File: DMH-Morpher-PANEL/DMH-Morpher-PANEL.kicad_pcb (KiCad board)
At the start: 2 copper layers, 50 x 200 mm, 4 parts

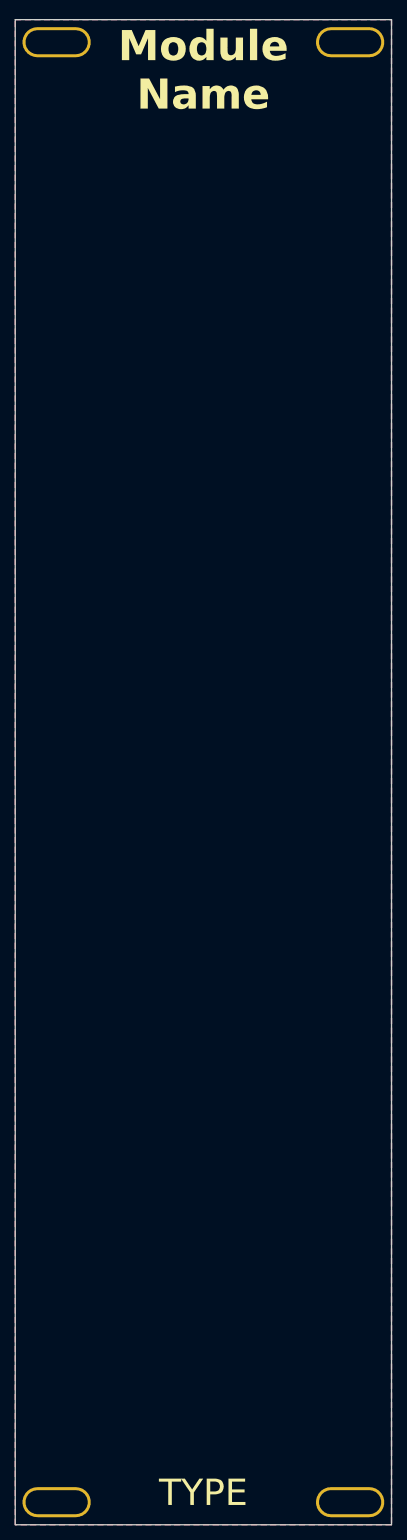
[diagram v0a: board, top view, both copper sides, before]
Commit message: Designed panel
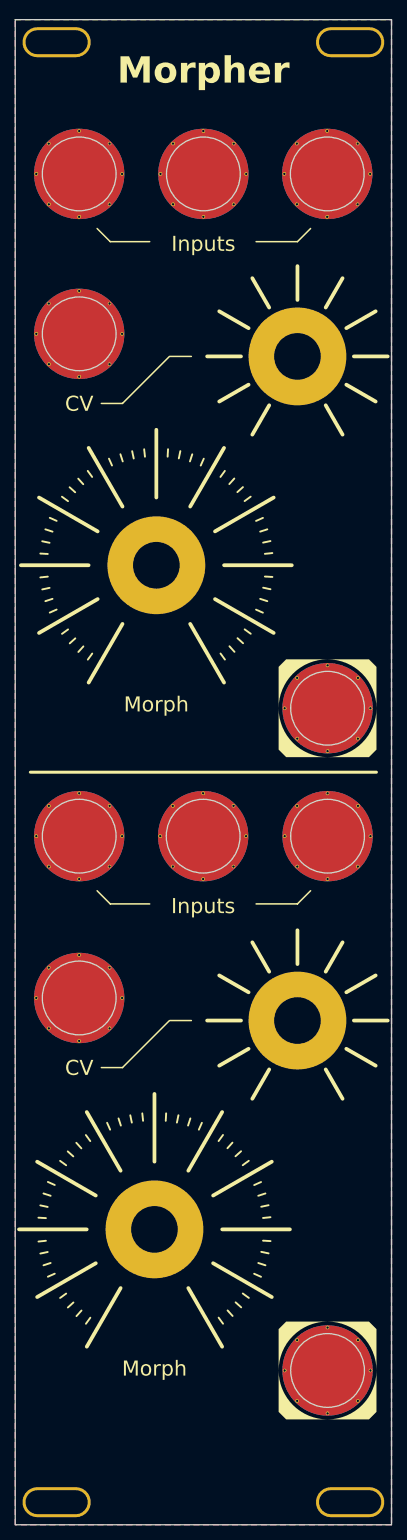
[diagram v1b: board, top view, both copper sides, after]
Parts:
- added H10: Morph, SynthStuff:Pot_Cutout_Medium_v2, F.Cu at (68.8, 102.5)
- added H11: CV A Amount, SynthStuff:Pot_Cutout_Tiny, F.Cu at (87.5, 74.8)
- added H12: In B1, SynthStuff:Jack_6.35mm_Cutout_v3, F.Cu at (58.5, 138.5)
- added H13: Out B, SynthStuff:Jack_6.35mm_Cutout_Output_v6, F.Cu at (91.5, 209.5)
- added H14: Morph, SynthStuff:Pot_Cutout_Medium_v2, F.Cu at (68.5, 190.8)
- added H15: Inputs, SynthStuff:Jack_6.35mm_Cutout_v3, F.Cu at (75.0, 138.5)
- added H16: CV B Amount, SynthStuff:Pot_Cutout_Tiny, F.Cu at (87.5, 163.0)
- added H17: In B3, SynthStuff:Jack_6.35mm_Cutout_v3, F.Cu at (91.5, 138.5)
- added H18: CV, SynthStuff:Jack_6.35mm_Cutout_v3, F.Cu at (58.5, 160.0)
- added H5: In A1, SynthStuff:Jack_6.35mm_Cutout_v3, F.Cu at (58.5, 50.5)
- added H6: Inputs, SynthStuff:Jack_6.35mm_Cutout_v3, F.Cu at (75.0, 50.5)
- added H7: In A3, SynthStuff:Jack_6.35mm_Cutout_v3, F.Cu at (91.5, 50.5)
- added H8: Output, SynthStuff:Jack_6.35mm_Cutout_Output_v6, F.Cu at (91.5, 121.5)
- added H9: CV, SynthStuff:Jack_6.35mm_Cutout_v3, F.Cu at (58.5, 71.8)
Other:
- board text added: "Morpher"
- board text removed: "Module Name"
